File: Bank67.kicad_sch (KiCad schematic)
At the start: 1 part, among them U1 XCKU5P-FFVB676

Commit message: finishing schematic
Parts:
- added R63: 240, Resistor_SMD:R_0201_0603Metric, symbol Device:R
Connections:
- net IO_L17N_T2U_N9_AD10N_67_N: now reaches U1.A15 (IO_L17N_T2U_N9_AD10N_67_N)
- net IO_L16P_T2U_N6_QBC_AD3P_67_P: now reaches U1.A17 (IO_L16P_T2U_N6_QBC_AD3P_67_P)
- net IO_L16N_T2U_N7_QBC_AD3N_67_N: now reaches U1.A18 (IO_L16N_T2U_N7_QBC_AD3N_67_N)
- net IO_L18P_T2U_N10_AD2P_67_P: now reaches U1.A19 (IO_L18P_T2U_N10_AD2P_67_P)
- net IO_L18N_T2U_N11_AD2N_67_N: now reaches U1.A20 (IO_L18N_T2U_N11_AD2N_67_N)
- net IO_L19P_T3L_N0_DBC_AD9P_67_P: now reaches U1.A22 (IO_L19P_T3L_N0_DBC_AD9P_67_P)
- net IO_L19N_T3L_N1_DBC_AD9N_67_N: now reaches U1.A23 (IO_L19N_T3L_N1_DBC_AD9N_67_N)
- net IO_L23P_T3U_N8_67_P: now reaches U1.A24 (IO_L23P_T3U_N8_67_P)
- net IO_L23N_T3U_N9_67_N: now reaches U1.A25 (IO_L23N_T3U_N9_67_N)
- net IO_L17P_T2U_N8_AD10P_67_P: now reaches U1.B15 (IO_L17P_T2U_N8_AD10P_67_P)
- net IO_T2U_N12_67: now reaches U1.B16 (IO_T2U_N12_67)
- net IO_L15N_T2L_N5_AD11N_67_N: now reaches U1.B17 (IO_L15N_T2L_N5_AD11N_67_N)
- net IO_L14P_T2L_N2_GC_67_P: now reaches U1.B19 (IO_L14P_T2L_N2_GC_67_P)
- net IO_L14N_T2L_N3_GC_67_N: now reaches U1.B20 (IO_L14N_T2L_N3_GC_67_N)
- net IO_L22N_T3U_N7_DBC_AD0N_67_N: now reaches U1.B21 (IO_L22N_T3U_N7_DBC_AD0N_67_N)
- net IO_L24N_T3U_N11_67_N: now reaches U1.B22 (IO_L24N_T3U_N11_67_N)
- net IO_L21N_T3L_N5_AD8N_67_N: now reaches U1.B24 (IO_L21N_T3L_N5_AD8N_67_N)
- net IO_L6N_T0U_N11_AD6N_67_N: now reaches U1.C16 (IO_L6N_T0U_N11_AD6N_67_N)
- net IO_L15P_T2L_N4_AD11P_67_P: now reaches U1.C17 (IO_L15P_T2L_N4_AD11P_67_P)
- net IO_L13P_T2L_N0_GC_QBC_67_P: now reaches U1.C18 (IO_L13P_T2L_N0_GC_QBC_67_P)
- net IO_L13N_T2L_N1_GC_QBC_67_N: now reaches U1.C19 (IO_L13N_T2L_N1_GC_QBC_67_N)
- net IO_L22P_T3U_N6_DBC_AD0P_67_P: now reaches U1.C21 (IO_L22P_T3U_N6_DBC_AD0P_67_P)
- net IO_L24P_T3U_N10_67_P: now reaches U1.C22 (IO_L24P_T3U_N10_67_P)
- net IO_L21P_T3L_N4_AD8P_67_P: now reaches U1.C23 (IO_L21P_T3L_N4_AD8P_67_P)
- net IO_L3N_T0L_N5_AD15N_67_N: now reaches U1.D15 (IO_L3N_T0L_N5_AD15N_67_N)
- net IO_L6P_T0U_N10_AD6P_67_P: now reaches U1.D16 (IO_L6P_T0U_N10_AD6P_67_P)
- net IO_L11N_T1U_N9_GC_67_N: now reaches U1.D18 (IO_L11N_T1U_N9_GC_67_N)
- net IO_L12P_T1U_N10_GC_67_P: now reaches U1.D19 (IO_L12P_T1U_N10_GC_67_P)
- net IO_L12N_T1U_N11_GC_67_N: now reaches U1.D20 (IO_L12N_T1U_N11_GC_67_N)
- net IO_L20N_T3L_N3_AD1N_67_N: now reaches U1.D21 (IO_L20N_T3L_N3_AD1N_67_N)
- net IO_L3P_T0L_N4_AD15P_67_P: now reaches U1.E15 (IO_L3P_T0L_N4_AD15P_67_P)
- net IO_L4P_T0U_N6_DBC_AD7P_67_P: now reaches U1.E16 (IO_L4P_T0U_N6_DBC_AD7P_67_P)
- net IO_L4N_T0U_N7_DBC_AD7N_67_N: now reaches U1.E17 (IO_L4N_T0U_N7_DBC_AD7N_67_N)
- net IO_L11P_T1U_N8_GC_67_P: now reaches U1.E18 (IO_L11P_T1U_N8_GC_67_P)
- net IO_L10N_T1U_N7_QBC_AD4N_67_N: now reaches U1.E20 (IO_L10N_T1U_N7_QBC_AD4N_67_N)
- net IO_L20P_T3L_N2_AD1P_67_P: now reaches U1.E21 (IO_L20P_T3L_N2_AD1P_67_P)
- net IO_T3U_N12_67: now reaches U1.E22 (IO_T3U_N12_67)
- net IO_L1N_T0L_N1_DBC_67_N: now reaches U1.F15 (IO_L1N_T0L_N1_DBC_67_N)
- net VRP: now reaches U1.F17 (IO_T0U_N12_VRP_67)
- net VRP: now also R63.1
- net IO_L8P_T1L_N2_AD5P_67_P: now reaches U1.F18 (IO_L8P_T1L_N2_AD5P_67_P)
- net IO_L8N_T1L_N3_AD5N_67_N: now reaches U1.F19 (IO_L8N_T1L_N3_AD5N_67_N)
- net IO_L10P_T1U_N6_QBC_AD4P_67_P: now reaches U1.F20 (IO_L10P_T1U_N6_QBC_AD4P_67_P)
- net IO_L1P_T0L_N0_DBC_67_P: now reaches U1.G15 (IO_L1P_T0L_N0_DBC_67_P)
- net IO_L5N_T0U_N9_AD14N_67_N: now reaches U1.G16 (IO_L5N_T0U_N9_AD14N_67_N)
- net IO_L2N_T0L_N3_67_N: now reaches U1.G17 (IO_L2N_T0L_N3_67_N)
- net IO_T1U_N12_67: now reaches U1.G19 (IO_T1U_N12_67)
- net IO_L9P_T1L_N4_AD12P_67_P: now reaches U1.G20 (IO_L9P_T1L_N4_AD12P_67_P)
- net IO_L9N_T1L_N5_AD12N_67_N: now reaches U1.G21 (IO_L9N_T1L_N5_AD12N_67_N)
- net IO_L5P_T0U_N8_AD14P_67_P: now reaches U1.H16 (IO_L5P_T0U_N8_AD14P_67_P)
- net IO_L2P_T0L_N2_67_P: now reaches U1.H17 (IO_L2P_T0L_N2_67_P)
- net IO_L7P_T1L_N0_QBC_AD13P_67_P: now reaches U1.H18 (IO_L7P_T1L_N0_QBC_AD13P_67_P)
- net IO_L7N_T1L_N1_QBC_AD13N_67_N: now reaches U1.H19 (IO_L7N_T1L_N1_QBC_AD13N_67_N)
- new net GND: R63.2

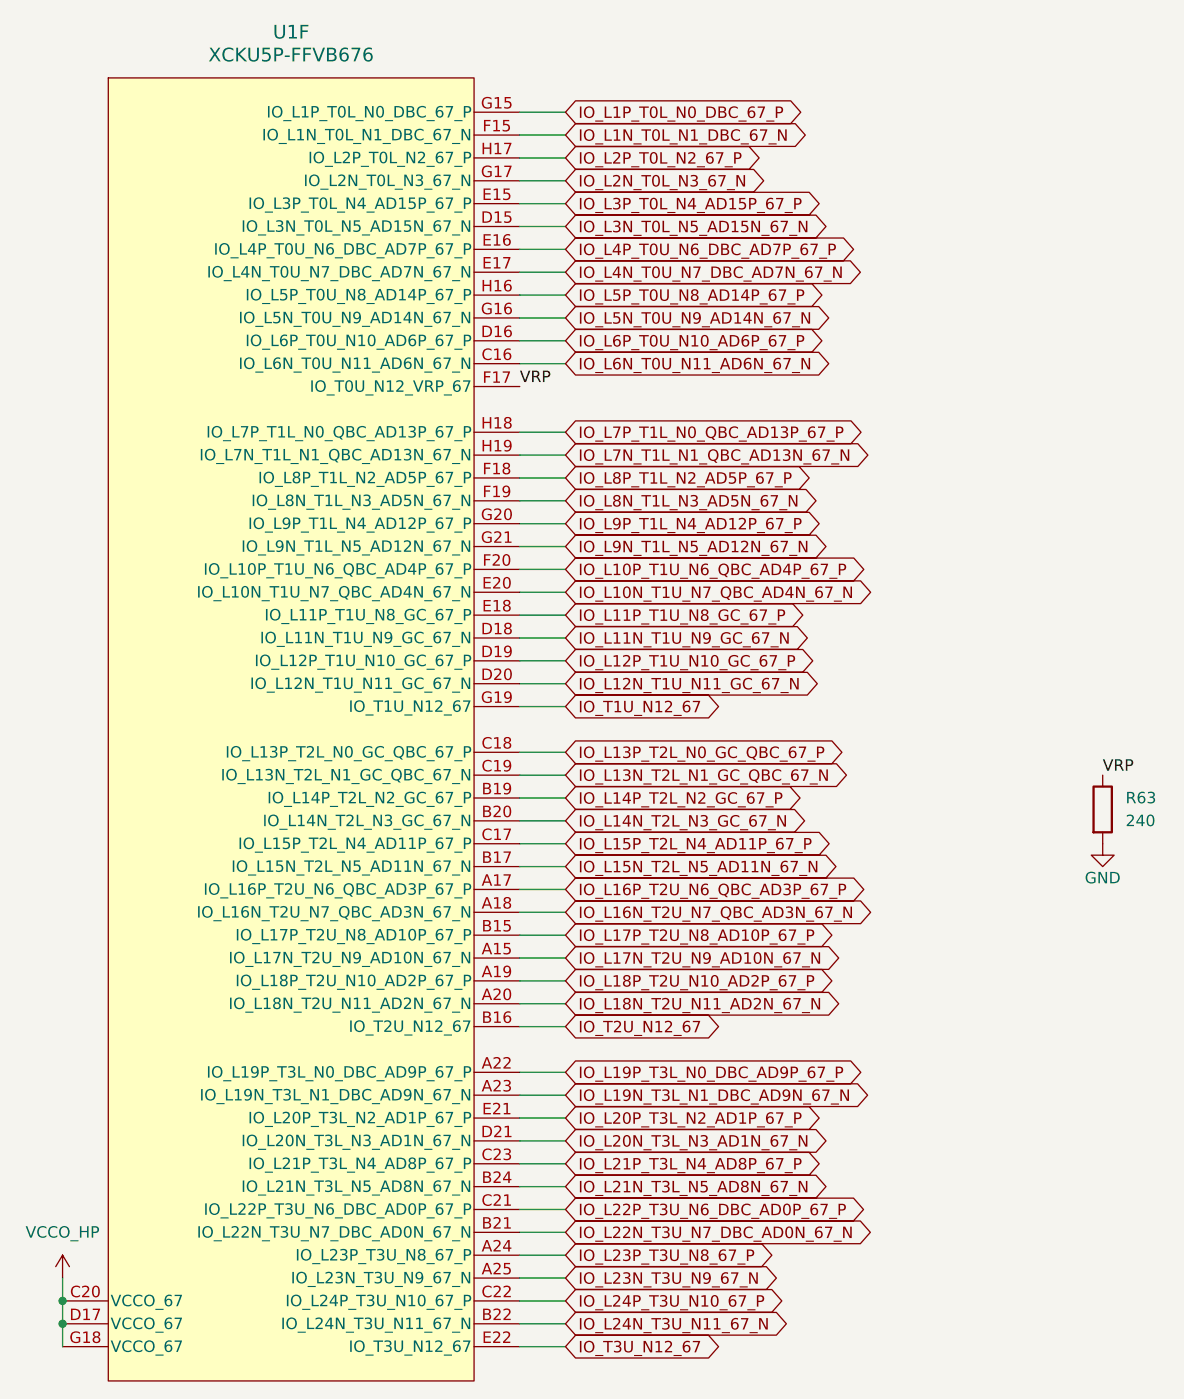
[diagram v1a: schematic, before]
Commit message: change net name to of IO diff pairs, add a scripts for name modification
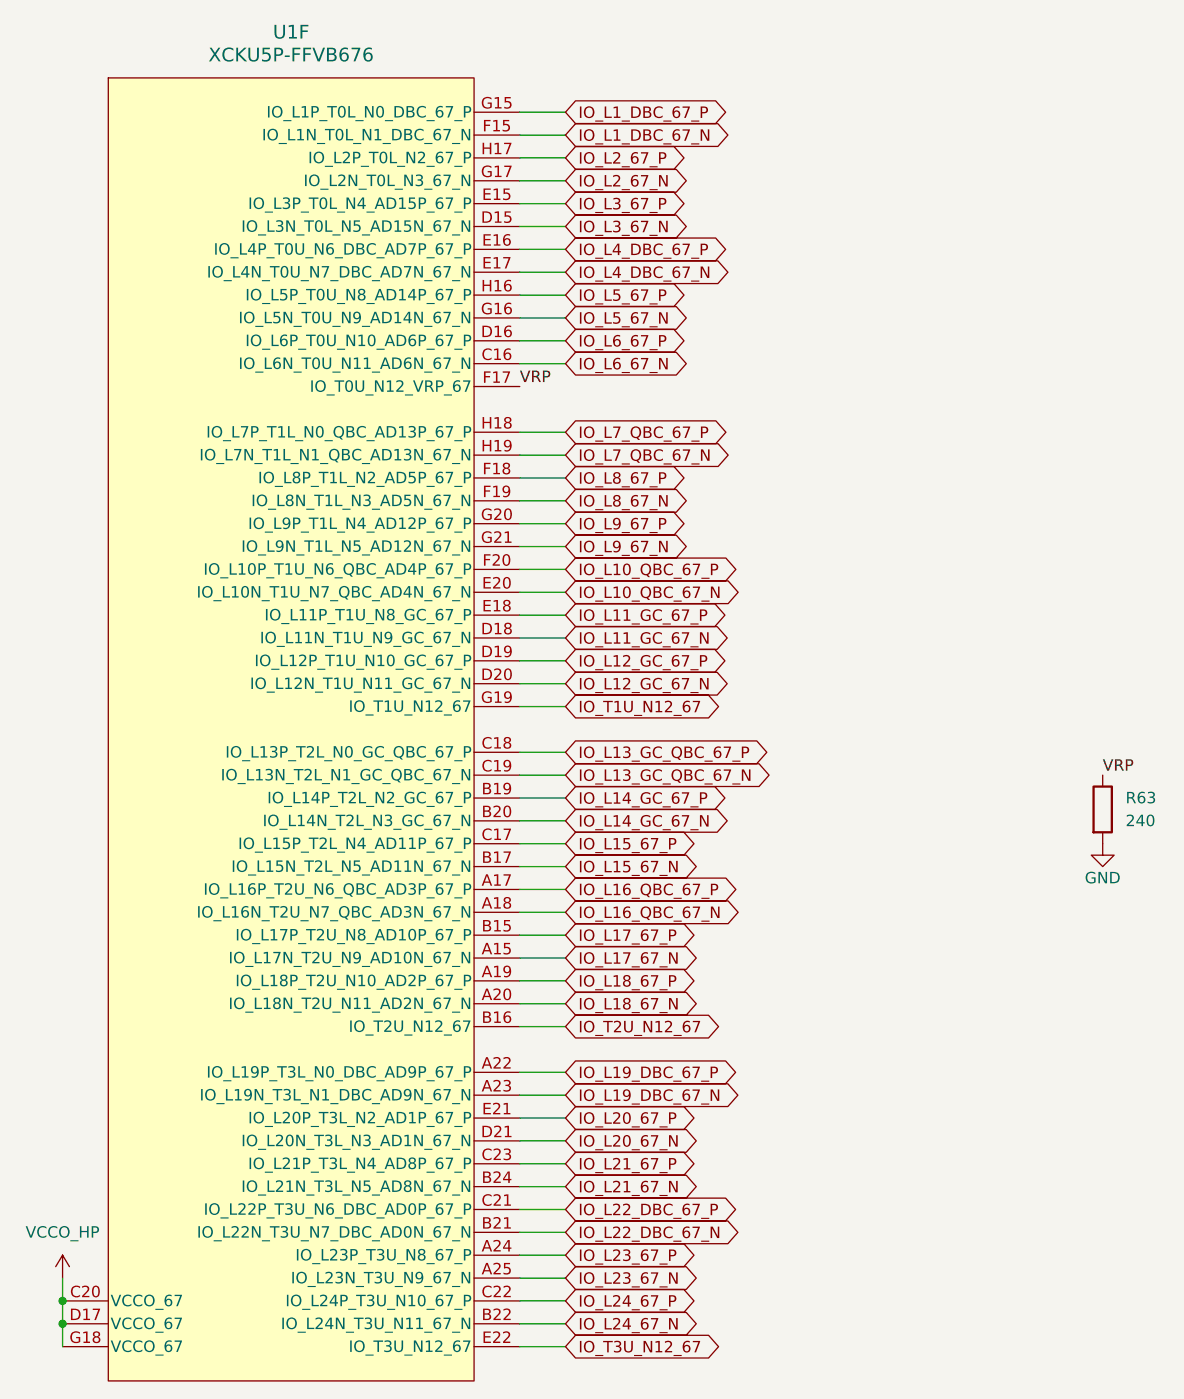
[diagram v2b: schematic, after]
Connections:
- net IO_L10N_T1U_N7_QBC_AD4N_67_N renamed IO_L10_QBC_67_N
- net IO_L10P_T1U_N6_QBC_AD4P_67_P renamed IO_L10_QBC_67_P
- net IO_L11N_T1U_N9_GC_67_N renamed IO_L11_GC_67_N
- net IO_L11P_T1U_N8_GC_67_P renamed IO_L11_GC_67_P
- net IO_L12N_T1U_N11_GC_67_N renamed IO_L12_GC_67_N
- net IO_L12P_T1U_N10_GC_67_P renamed IO_L12_GC_67_P
- net IO_L13N_T2L_N1_GC_QBC_67_N renamed IO_L13_GC_QBC_67_N
- net IO_L13P_T2L_N0_GC_QBC_67_P renamed IO_L13_GC_QBC_67_P
- net IO_L14N_T2L_N3_GC_67_N renamed IO_L14_GC_67_N
- net IO_L14P_T2L_N2_GC_67_P renamed IO_L14_GC_67_P
- net IO_L15N_T2L_N5_AD11N_67_N renamed IO_L15_67_N
- net IO_L15P_T2L_N4_AD11P_67_P renamed IO_L15_67_P
- net IO_L16N_T2U_N7_QBC_AD3N_67_N renamed IO_L16_QBC_67_N
- net IO_L16P_T2U_N6_QBC_AD3P_67_P renamed IO_L16_QBC_67_P
- net IO_L17N_T2U_N9_AD10N_67_N renamed IO_L17_67_N
- net IO_L17P_T2U_N8_AD10P_67_P renamed IO_L17_67_P
- net IO_L18N_T2U_N11_AD2N_67_N renamed IO_L18_67_N
- net IO_L18P_T2U_N10_AD2P_67_P renamed IO_L18_67_P
- net IO_L19N_T3L_N1_DBC_AD9N_67_N renamed IO_L19_DBC_67_N
- net IO_L19P_T3L_N0_DBC_AD9P_67_P renamed IO_L19_DBC_67_P
- net IO_L1N_T0L_N1_DBC_67_N renamed IO_L1_DBC_67_N
- net IO_L1P_T0L_N0_DBC_67_P renamed IO_L1_DBC_67_P
- net IO_L20N_T3L_N3_AD1N_67_N renamed IO_L20_67_N
- net IO_L20P_T3L_N2_AD1P_67_P renamed IO_L20_67_P
- net IO_L21N_T3L_N5_AD8N_67_N renamed IO_L21_67_N
- net IO_L21P_T3L_N4_AD8P_67_P renamed IO_L21_67_P
- net IO_L22N_T3U_N7_DBC_AD0N_67_N renamed IO_L22_DBC_67_N
- net IO_L22P_T3U_N6_DBC_AD0P_67_P renamed IO_L22_DBC_67_P
- net IO_L23N_T3U_N9_67_N renamed IO_L23_67_N
- net IO_L23P_T3U_N8_67_P renamed IO_L23_67_P
- net IO_L24N_T3U_N11_67_N renamed IO_L24_67_N
- net IO_L24P_T3U_N10_67_P renamed IO_L24_67_P
- net IO_L2N_T0L_N3_67_N renamed IO_L2_67_N
- net IO_L2P_T0L_N2_67_P renamed IO_L2_67_P
- net IO_L3N_T0L_N5_AD15N_67_N renamed IO_L3_67_N
- net IO_L3P_T0L_N4_AD15P_67_P renamed IO_L3_67_P
- net IO_L4N_T0U_N7_DBC_AD7N_67_N renamed IO_L4_DBC_67_N
- net IO_L4P_T0U_N6_DBC_AD7P_67_P renamed IO_L4_DBC_67_P
- net IO_L5N_T0U_N9_AD14N_67_N renamed IO_L5_67_N
- net IO_L5P_T0U_N8_AD14P_67_P renamed IO_L5_67_P
- net IO_L6N_T0U_N11_AD6N_67_N renamed IO_L6_67_N
- net IO_L6P_T0U_N10_AD6P_67_P renamed IO_L6_67_P
- net IO_L7N_T1L_N1_QBC_AD13N_67_N renamed IO_L7_QBC_67_N
- net IO_L7P_T1L_N0_QBC_AD13P_67_P renamed IO_L7_QBC_67_P
- net IO_L8N_T1L_N3_AD5N_67_N renamed IO_L8_67_N
- net IO_L8P_T1L_N2_AD5P_67_P renamed IO_L8_67_P
- net IO_L9N_T1L_N5_AD12N_67_N renamed IO_L9_67_N
- net IO_L9P_T1L_N4_AD12P_67_P renamed IO_L9_67_P
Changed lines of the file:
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@@
 		)
 	)
-	(global_label "IO_L15P_T2L_N4_AD11P_67_P"
+	(global_label "IO_L15_67_P"
 		(shape bidirectional)
 		(at 113.03 115.57 0)
@@
 		)
 	)
-	(global_label "IO_L3N_T0L_N5_AD15N_67_N"
+	(global_label "IO_L3_67_N"
 		(shape bidirectional)
 		(at 113.03 46.99 0)
@@
 		)
 	)
-	(global_label "IO_L7N_T1L_N1_QBC_AD13N_67_N"
+	(global_label "IO_L7_QBC_67_N"
 		(shape bidirectional)
 		(at 113.03 72.39 0)
@@
 		)
 	)
-	(global_label "IO_L4N_T0U_N7_DBC_AD7N_67_N"
+	(global_label "IO_L4_DBC_67_N"
 		(shape bidirectional)
 		(at 113.03 52.07 0)
@@
 		)
 	)
-	(global_label "IO_L23N_T3U_N9_67_N"
+	(global_label "IO_L23_67_N"
 		(shape bidirectional)
 		(at 113.03 163.83 0)
@@
 		)
 	)
-	(global_label "IO_L6N_T0U_N11_AD6N_67_N"
+	(global_label "IO_L6_67_N"
 		(shape bidirectional)
 		(at 113.03 62.23 0)
@@
 		)
 	)
-	(global_label "IO_L21P_T3L_N4_AD8P_67_P"
+	(global_label "IO_L21_67_P"
 		(shape bidirectional)
 		(at 113.03 151.13 0)
@@
 		)
 	)
-	(global_label "IO_L16N_T2U_N7_QBC_AD3N_67_N"
+	(global_label "IO_L16_QBC_67_N"
 		(shape bidirectional)
 		(at 113.03 123.19 0)
@@
 		)
 	)
-	(global_label "IO_L8N_T1L_N3_AD5N_67_N"
+	(global_label "IO_L8_67_N"
 		(shape bidirectional)
 		(at 113.03 77.47 0)
@@
 		)
 	)
-	(global_label "IO_L10P_T1U_N6_QBC_AD4P_67_P"
+	(global_label "IO_L10_QBC_67_P"
 		(shape bidirectional)
 		(at 113.03 85.09 0)
@@
 		)
 	)
-	(global_label "IO_L1P_T0L_N0_DBC_67_P"
+	(global_label "IO_L1_DBC_67_P"
 		(shape bidirectional)
 		(at 113.03 34.29 0)
@@
 		)
 	)
-	(global_label "IO_L18P_T2U_N10_AD2P_67_P"
+	(global_label "IO_L18_67_P"
 		(shape bidirectional)
 		(at 113.03 130.81 0)
@@
 		)
 	)
-	(global_label "IO_L20N_T3L_N3_AD1N_67_N"
+	(global_label "IO_L20_67_N"
 		(shape bidirectional)
 		(at 113.03 148.59 0)
@@
 		)
 	)
-	(global_label "IO_L20P_T3L_N2_AD1P_67_P"
+	(global_label "IO_L20_67_P"
 		(shape bidirectional)
 		(at 113.03 146.05 0)
@@
 		)
 	)
-	(global_label "IO_L22N_T3U_N7_DBC_AD0N_67_N"
+	(global_label "IO_L22_DBC_67_N"
 		(shape bidirectional)
 		(at 113.03 158.75 0)
@@
 		)
 	)
-	(global_label "IO_L9N_T1L_N5_AD12N_67_N"
+	(global_label "IO_L9_67_N"
 		(shape bidirectional)
 		(at 113.03 82.55 0)
@@
 		)
 	)
-	(global_label "IO_L15N_T2L_N5_AD11N_67_N"
+	(global_label "IO_L15_67_N"
 		(shape bidirectional)
 		(at 113.03 118.11 0)
@@
 		)
 	)
-	(global_label "IO_L14N_T2L_N3_GC_67_N"
+	(global_label "IO_L14_GC_67_N"
 		(shape bidirectional)
 		(at 113.03 113.03 0)
@@
 		)
 	)
-	(global_label "IO_L19N_T3L_N1_DBC_AD9N_67_N"
+	(global_label "IO_L19_DBC_67_N"
 		(shape bidirectional)
 		(at 113.03 143.51 0)
@@
 		)
 	)
-	(global_label "IO_L17P_T2U_N8_AD10P_67_P"
+	(global_label "IO_L17_67_P"
 		(shape bidirectional)
 		(at 113.03 125.73 0)
@@
 		)
 	)
-	(global_label "IO_L21N_T3L_N5_AD8N_67_N"
+	(global_label "IO_L21_67_N"
 		(shape bidirectional)
 		(at 113.03 153.67 0)
@@
 		)
 	)
-	(global_label "IO_L5N_T0U_N9_AD14N_67_N"
+	(global_label "IO_L5_67_N"
 		(shape bidirectional)
 		(at 113.03 57.15 0)
@@
 		)
 	)
-	(global_label "IO_L18N_T2U_N11_AD2N_67_N"
+	(global_label "IO_L18_67_N"
 		(shape bidirectional)
 		(at 113.03 133.35 0)
@@
 		)
 	)
-	(global_label "IO_L8P_T1L_N2_AD5P_67_P"
+	(global_label "IO_L8_67_P"
 		(shape bidirectional)
 		(at 113.03 74.93 0)
@@
 		)
 	)
-	(global_label "IO_L19P_T3L_N0_DBC_AD9P_67_P"
+	(global_label "IO_L19_DBC_67_P"
 		(shape bidirectional)
 		(at 113.03 140.97 0)
@@
 		)
 	)
-	(global_label "IO_L11N_T1U_N9_GC_67_N"
+	(global_label "IO_L11_GC_67_N"
 		(shape bidirectional)
 		(at 113.03 92.71 0)
@@
 		)
 	)
-	(global_label "IO_L2N_T0L_N3_67_N"
+	(global_label "IO_L2_67_N"
 		(shape bidirectional)
 		(at 113.03 41.91 0)
@@
 		)
 	)
-	(global_label "IO_L3P_T0L_N4_AD15P_67_P"
+	(global_label "IO_L3_67_P"
 		(shape bidirectional)
 		(at 113.03 44.45 0)
@@
 		)
 	)
-	(global_label "IO_L12N_T1U_N11_GC_67_N"
+	(global_label "IO_L12_GC_67_N"
 		(shape bidirectional)
 		(at 113.03 97.79 0)
@@
 		)
 	)
-	(global_label "IO_L13N_T2L_N1_GC_QBC_67_N"
+	(global_label "IO_L13_GC_QBC_67_N"
 		(shape bidirectional)
 		(at 113.03 107.95 0)
@@
 		)
 	)
-	(global_label "IO_L2P_T0L_N2_67_P"
+	(global_label "IO_L2_67_P"
 		(shape bidirectional)
 		(at 113.03 39.37 0)
@@
 		)
 	)
-	(global_label "IO_L12P_T1U_N10_GC_67_P"
+	(global_label "IO_L12_GC_67_P"
 		(shape bidirectional)
 		(at 113.03 95.25 0)
@@
 		)
 	)
-	(global_label "IO_L5P_T0U_N8_AD14P_67_P"
+	(global_label "IO_L5_67_P"
 		(shape bidirectional)
 		(at 113.03 54.61 0)
@@
 		)
 	)
-	(global_label "IO_L22P_T3U_N6_DBC_AD0P_67_P"
+	(global_label "IO_L22_DBC_67_P"
 		(shape bidirectional)
 		(at 113.03 156.21 0)
@@
 		)
 	)
-	(global_label "IO_L4P_T0U_N6_DBC_AD7P_67_P"
+	(global_label "IO_L4_DBC_67_P"
 		(shape bidirectional)
 		(at 113.03 49.53 0)
@@
 		)
 	)
-	(global_label "IO_L11P_T1U_N8_GC_67_P"
+	(global_label "IO_L11_GC_67_P"
 		(shape bidirectional)
 		(at 113.03 90.17 0)
@@
 		)
 	)
-	(global_label "IO_L1N_T0L_N1_DBC_67_N"
+	(global_label "IO_L1_DBC_67_N"
 		(shape bidirectional)
 		(at 113.03 36.83 0)
@@
 		)
 	)
-	(global_label "IO_L16P_T2U_N6_QBC_AD3P_67_P"
+	(global_label "IO_L16_QBC_67_P"
 		(shape bidirectional)
 		(at 113.03 120.65 0)
@@
 		)
 	)
-	(global_label "IO_L17N_T2U_N9_AD10N_67_N"
+	(global_label "IO_L17_67_N"
 		(shape bidirectional)
 		(at 113.03 128.27 0)
@@
 		)
 	)
-	(global_label "IO_L6P_T0U_N10_AD6P_67_P"
+	(global_label "IO_L6_67_P"
 		(shape bidirectional)
 		(at 113.03 59.69 0)
@@
 		)
 	)
-	(global_label "IO_L23P_T3U_N8_67_P"
+	(global_label "IO_L23_67_P"
 		(shape bidirectional)
 		(at 113.03 161.29 0)
@@
 		)
 	)
-	(global_label "IO_L10N_T1U_N7_QBC_AD4N_67_N"
+	(global_label "IO_L10_QBC_67_N"
 		(shape bidirectional)
 		(at 113.03 87.63 0)
@@
 		)
 	)
-	(global_label "IO_L24P_T3U_N10_67_P"
+	(global_label "IO_L24_67_P"
 		(shape bidirectional)
 		(at 113.03 166.37 0)
@@
 		)
 	)
-	(global_label "IO_L14P_T2L_N2_GC_67_P"
+	(global_label "IO_L14_GC_67_P"
 		(shape bidirectional)
 		(at 113.03 110.49 0)
@@
 		)
 	)
-	(global_label "IO_L24N_T3U_N11_67_N"
+	(global_label "IO_L24_67_N"
 		(shape bidirectional)
 		(at 113.03 168.91 0)
@@
 		)
 	)
-	(global_label "IO_L7P_T1L_N0_QBC_AD13P_67_P"
+	(global_label "IO_L7_QBC_67_P"
 		(shape bidirectional)
 		(at 113.03 69.85 0)
@@
 		)
 	)
-	(global_label "IO_L9P_T1L_N4_AD12P_67_P"
+	(global_label "IO_L9_67_P"
 		(shape bidirectional)
 		(at 113.03 80.01 0)
@@
 		)
 	)
-	(global_label "IO_L13P_T2L_N0_GC_QBC_67_P"
+	(global_label "IO_L13_GC_QBC_67_P"
 		(shape bidirectional)
 		(at 113.03 105.41 0)
